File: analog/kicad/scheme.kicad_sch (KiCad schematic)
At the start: 25 parts, among them J1 Barrel_Jack_Switch, U1 LM7805_TO220, U2 LM324

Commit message: more ai research + kicad schematic update
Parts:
- removed J1: Barrel_Jack_Switch, Connector_BarrelJack:BarrelJack_GCT_DCJ200-10-A_Horizontal, symbol Connector:Barrel_Jack_Switch
- removed R7: 1.6k, Resistor_SMD:R_0805_2012Metric, symbol Device:R
- removed R8: 4.7k, Resistor_SMD:R_0805_2012Metric, symbol Device:R
- added BT1: Battery_Cell 9V, Battery:BatteryClip_Keystone_54_D16-19mm, symbol Device:Battery_Cell
- added SW1: SW_Nidec_CAS-120A1, Button_Switch_SMD:Nidec_Copal_CAS-120A, symbol Switch:SW_Nidec_CAS-120A1
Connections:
- net +5V: now also R3.1; no longer R3.2
- net GND: now also C2.2, R1.2, U1.2 (GND), BT1.2 (-); no longer C2.1, R1.1
- net at C3.1, U1.1 (VI): now also SW1.3 (A)
- removed net BIAS: C2.2, R1.2, R3.1, U2.3 (+)
- net OUT renamed TIA_OUT
- net dist2 renamed (1.7V)
- net dist3 renamed (2.5V)
- new net: BT1.1 (+), SW1.2 (B)
- new net VGND: C2.1, R1.1, R3.2, U2.3 (+)
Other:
- note added: "Authors: Uko Poschlin Karl Romet de La Torre Jüri Kajava"
- moved on the sheet: C1, C2, C3, C4, C5, D1, D2, D3, D4, D5, R1, R10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

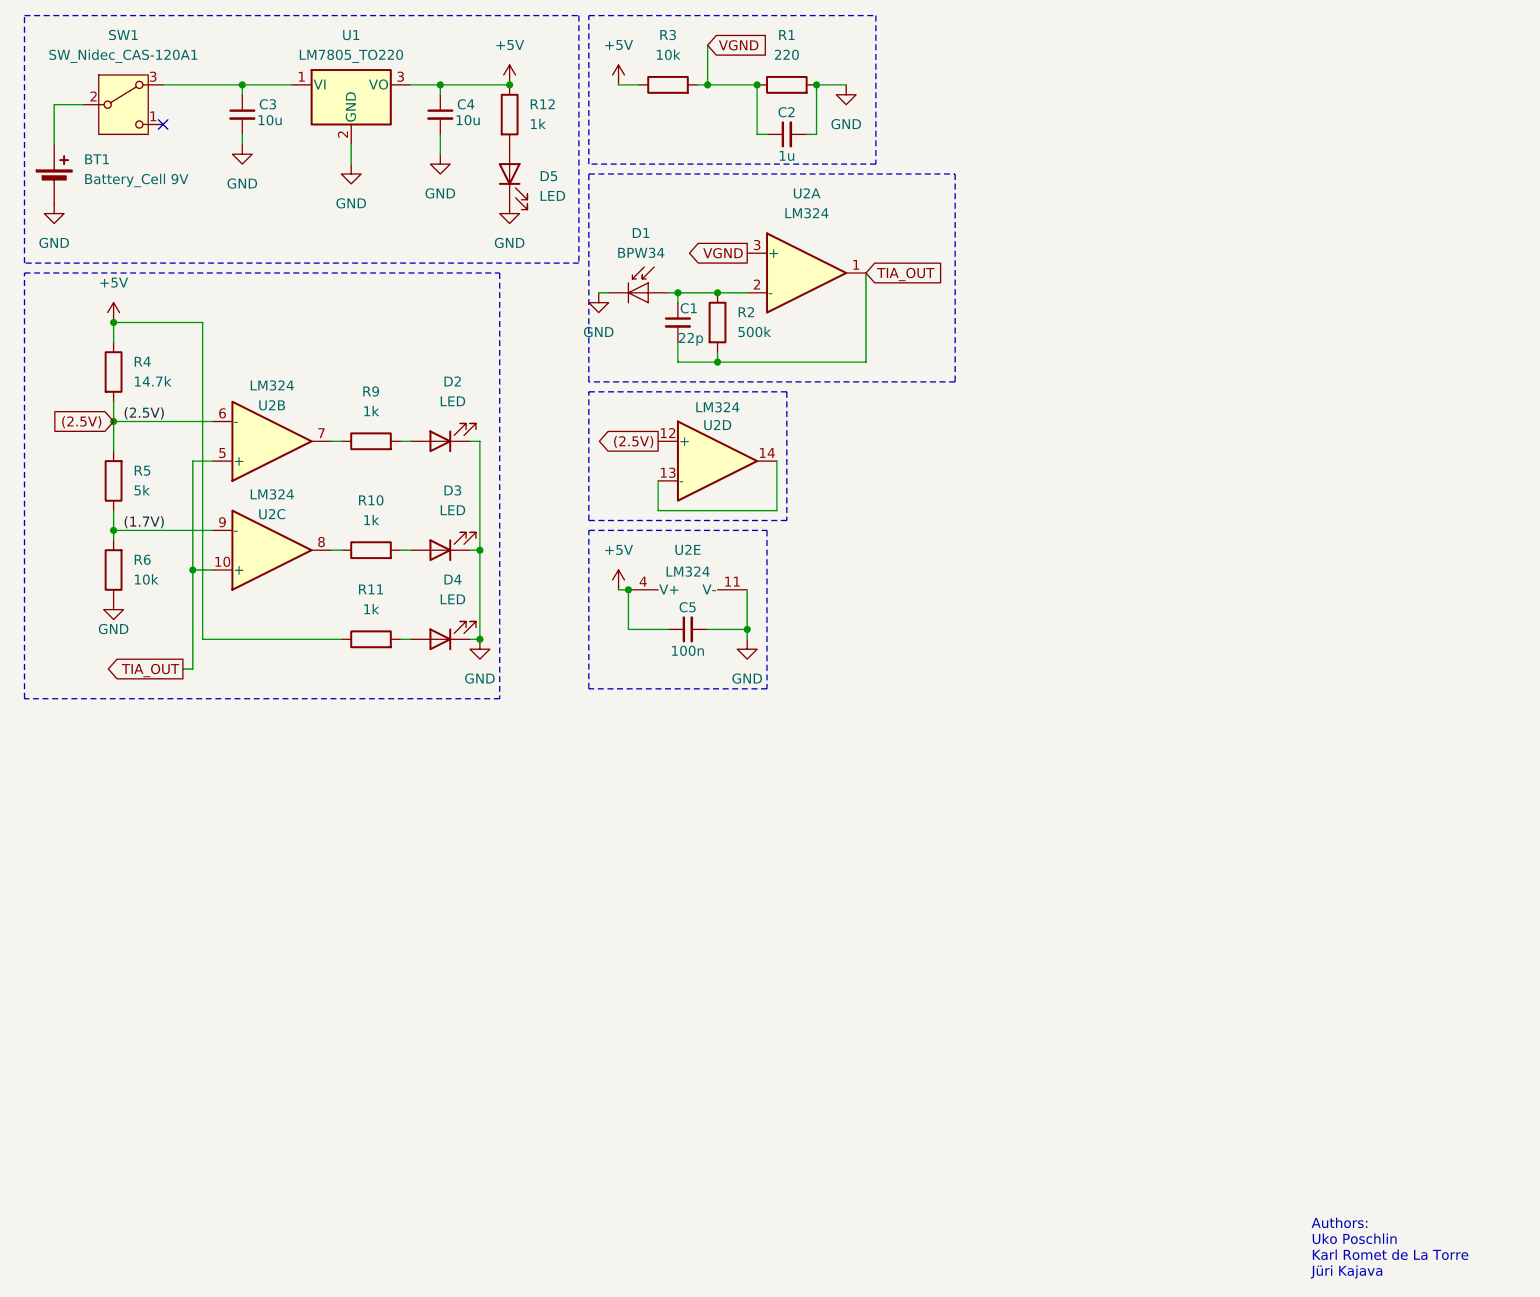
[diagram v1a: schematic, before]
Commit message: + fuse + tvs
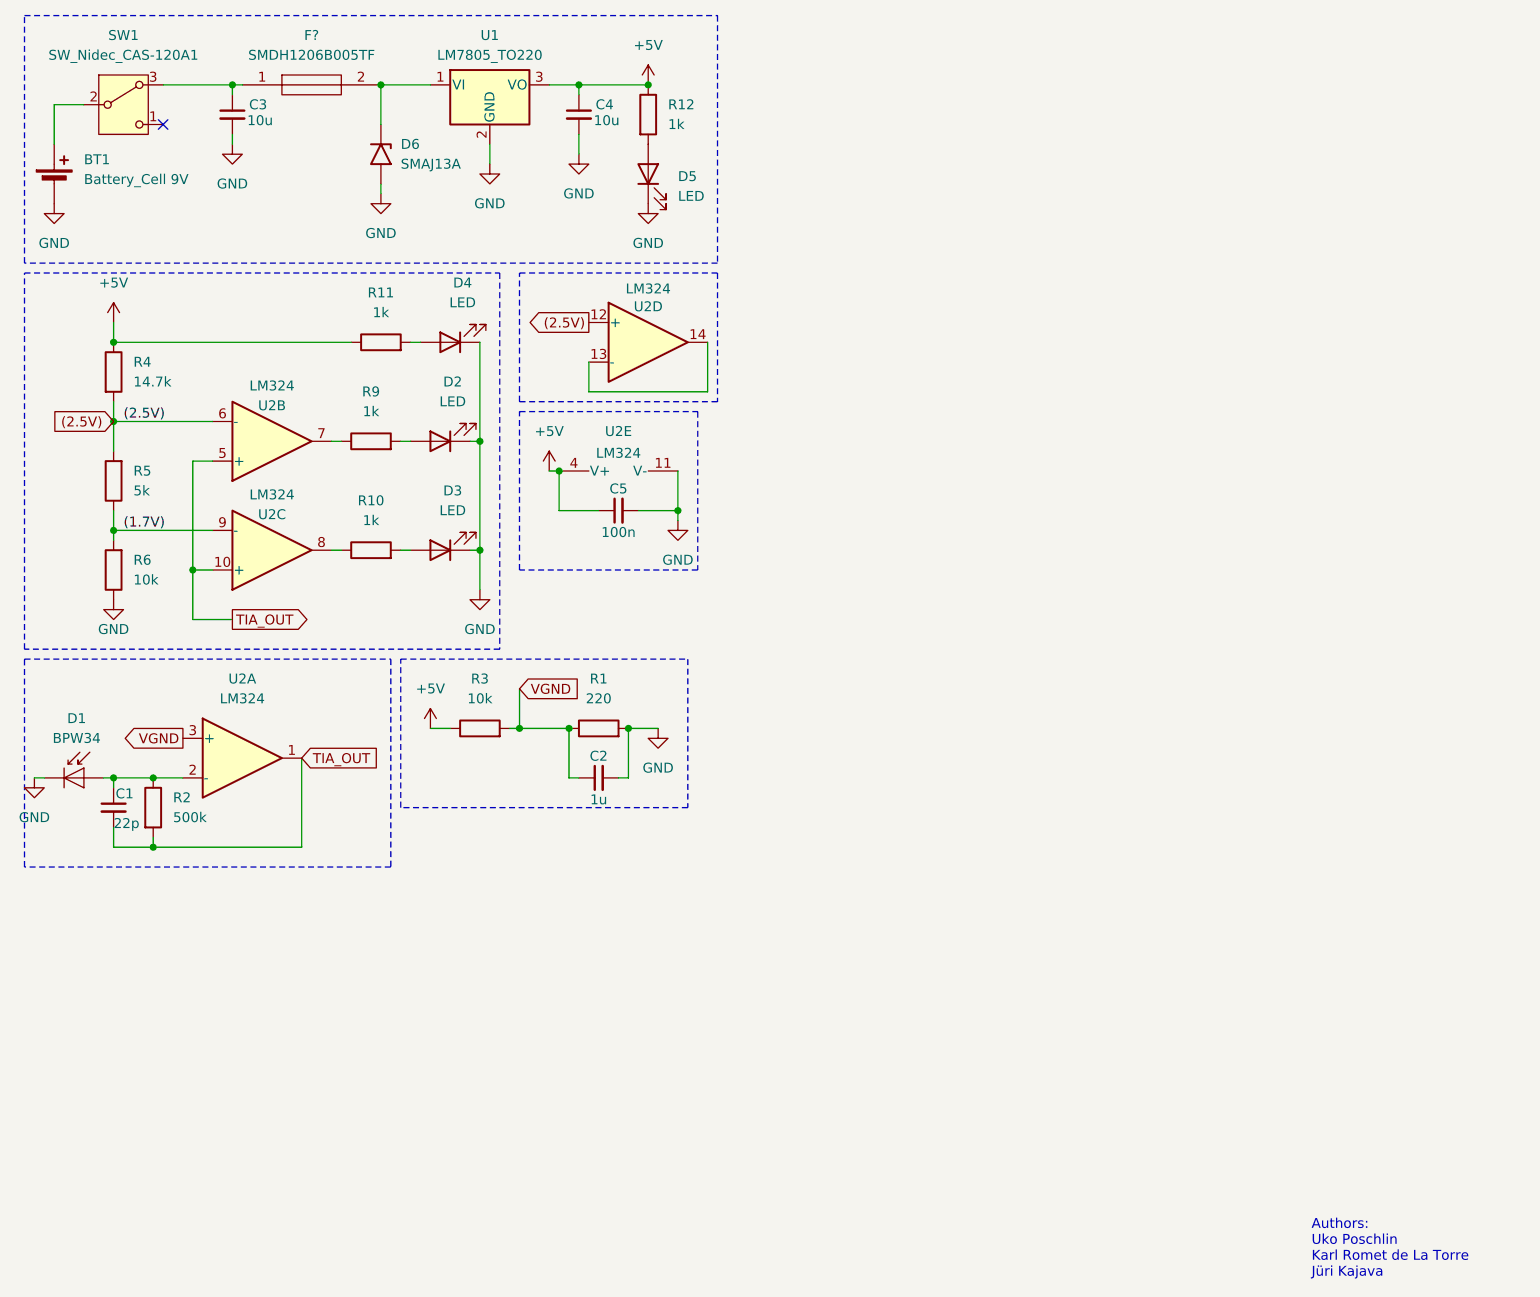
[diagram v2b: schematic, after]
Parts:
- added D6: SMAJ13A, Diode_SMD:D_SMA, symbol Diode:SMAJ13A
- added F?: SMDH1206B005TF, FUSC3216X115N, symbol IMPORT_LIB:SMDH1206B005TF
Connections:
- net GND: now also D6.2 (A2)
- net at C3.1, SW1.3 (A): now also F?.1; no longer U1.1 (VI)
- new net: D6.1 (A1), F?.2, U1.1 (VI)
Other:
- moved on the sheet: C1, C2, C3, C4, C5, D1, D4, D5, R1, R11, R12, R2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

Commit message: pcb changes
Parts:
- BT1: footprint Battery:BatteryClip_Keystone_54_D16-19mm -> Battery:BatteryHolder_Eagle_12BH611-GR
- F1: renamed from F?; footprint FUSC3216X115N -> Resistor_SMD:R_1206_3216Metric
- U2: footprint Package_DIP:DIP-14_W7.62mm_Socket -> Package_DIP:DIP-14_W7.62mm_SMDSocket_SmallPads
- renumbered R12 to R10, R9 to R7, R10 to R8, R11 to R9
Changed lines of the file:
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@@
 		(dnp no)
 		(fields_autoplaced yes)
-		(property "Reference" "R12"
+		(property "Reference" "R10"
 			(at 95.25 24.1299 0)
 			(effects
@@
 			(project ""
 				(path "/592a964a-3b7b-4079-9a16-282b0fdb7c03"
-					(reference "R12")
+					(reference "R10")
 					(unit 1)
 				)
@@
 		(dnp no)
 		(fields_autoplaced yes)
-		(property "Reference" "R10"
+		(property "Reference" "R8"
 			(at 57.15 74.93 90)
 			(effects
@@
 			(project "scheme"
 				(path "/592a964a-3b7b-4079-9a16-282b0fdb7c03"
-					(reference "R10")
+					(reference "R8")
 					(unit 1)
 				)
@@
 			)
 		)
-		(property "Footprint" "Battery:BatteryClip_Keystone_54_D16-19mm"
+		(property "Footprint" "Battery:BatteryHolder_Eagle_12BH611-GR"
 			(at 16.51 32.766 90)
 			(effects
@@
 			)
 		)
-		(property "Footprint" "Package_DIP:DIP-14_W7.62mm_Socket"
+		(property "Footprint" "Package_DIP:DIP-14_W7.62mm_SMDSocket_SmallPads"
 			(at 91.44 52.07 0)
 			(effects
@@
 		(dnp no)
 		(fields_autoplaced yes)
-		(property "Reference" "R11"
+		(property "Reference" "R9"
 			(at 58.42 48.26 90)
 			(effects
@@
 			(project "scheme"
 				(path "/592a964a-3b7b-4079-9a16-282b0fdb7c03"
-					(reference "R11")
+					(reference "R9")
 					(unit 1)
 				)
@@
 		(dnp no)
 		(fields_autoplaced yes)
-		(property "Reference" "F?"
+		(property "Reference" "F1"
 			(at 49.53 15.24 0)
 			(effects
@@
 			)
 		)
-		(property "Footprint" "FUSC3216X115N"
+		(property "Footprint" "Resistor_SMD:R_1206_3216Metric"
 			(at 54.61 20.32 0)
 			(effects
@@
 			(project ""
 				(path "/592a964a-3b7b-4079-9a16-282b0fdb7c03"
-					(reference "F?")
+					(reference "F1")
 					(unit 1)
 				)
@@
 			)
 		)
-		(property "Footprint" "Package_DIP:DIP-14_W7.62mm_Socket"
+		(property "Footprint" "Package_DIP:DIP-14_W7.62mm_SMDSocket_SmallPads"
 			(at 39.37 105.41 0)
 			(effects
@@
 			)
 		)
-		(property "Footprint" "Package_DIP:DIP-14_W7.62mm_Socket"
+		(property "Footprint" "Package_DIP:DIP-14_W7.62mm_SMDSocket_SmallPads"
 			(at 43.18 83.82 0)
 			(effects
@@
 		(dnp no)
 		(fields_autoplaced yes)
-		(property "Reference" "R9"
+		(property "Reference" "R7"
 			(at 57.15 60.96 90)
 			(effects
@@
 			(project "scheme"
 				(path "/592a964a-3b7b-4079-9a16-282b0fdb7c03"
-					(reference "R9")
+					(reference "R7")
 					(unit 1)
 				)
@@
 			)
 		)
-		(property "Footprint" "Package_DIP:DIP-14_W7.62mm_Socket"
+		(property "Footprint" "Package_DIP:DIP-14_W7.62mm_SMDSocket_SmallPads"
 			(at 43.18 69.85 0)
 			(effects
@@
 			)
 		)
-		(property "Footprint" "Package_DIP:DIP-14_W7.62mm_Socket"
+		(property "Footprint" "Package_DIP:DIP-14_W7.62mm_SMDSocket_SmallPads"
 			(at 86.36 69.85 0)
 			(effects

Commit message: more analog cleanup
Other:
- note removed: "Authors: Uko Poschlin Karl Romet de La Torre Jüri Kajava"
- company: (none) -> Uko Poschlin; Karl Romet de la Torre;
- title: (none) -> Valgustugevuse mõõtmine fotodioodiga 
- moved on the sheet: BT1, C1, C2, C3, C4, C5, D1, D2, D3, D4, D5, D6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

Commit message: pcb changes
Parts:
- D2, D3, D4: footprint LED_THT:LED_D5.0mm -> LED_THT:LED_D5.0mm_Horizontal_O1.27mm_Z3.0mm
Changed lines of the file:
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@@
 			)
 		)
-		(property "Footprint" "LED_THT:LED_D5.0mm"
+		(property "Footprint" "LED_THT:LED_D5.0mm_Horizontal_O1.27mm_Z3.0mm"
 			(at 82.55 107.95 0)
 			(effects
@@
 			)
 		)
-		(property "Footprint" "LED_THT:LED_D5.0mm"
+		(property "Footprint" "LED_THT:LED_D5.0mm_Horizontal_O1.27mm_Z3.0mm"
 			(at 82.55 121.92 0)
 			(effects
@@
 			)
 		)
-		(property "Footprint" "LED_THT:LED_D5.0mm"
+		(property "Footprint" "LED_THT:LED_D5.0mm_Horizontal_O1.27mm_Z3.0mm"
 			(at 83.82 95.25 0)
 			(effects

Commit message: bom changes
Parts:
- BT1: Mouser Price/Stock (none) -> 1,46
- C1, C2: Mouser Price/Stock (none) -> 0,10
- C3, C4: Mouser Price/Stock (none) -> 0,16
- C5: Mouser Price/Stock (none) -> 0,06
- D1: Mouser Price/Stock (none) -> 1,06
- D6: Mouser Price/Stock (none) -> 0,12
- F1: Mouser Price/Stock (none) -> 0,09
- SW1: Mouser Price/Stock (none) -> 1,26
- U1: Mouser Price/Stock (none) -> 1,55
- U2: Mouser Price/Stock (none) -> 0,404
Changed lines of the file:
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@@
+			)
+		)
+		(property "Mouser Price/Stock" "0,12"
+			(at 74.93 71.12 90)
+			(effects
+				(font
+					(size 1.27 1.27)
+				)
+				(hide yes)
 			)
 		)
@@
 			)
 		)
-		(property "Datasheet" "~"
+		(property "Datasheet" "https://mm.digikey.com/Volume0/opasdata/d220001/medias/docus/5660/3372_0805B105J250CC.pdf"
 			(at 102.87 151.13 0)
 			(effects
@@
 		(property "Description" "Unpolarized capacitor, small symbol"
 			(at 102.87 151.13 0)
+			(effects
+				(font
+					(size 1.27 1.27)
+				)
+				(hide yes)
+			)
+		)
+		(property "Mouser Price/Stock" "0,10"
+			(at 102.87 151.13 90)
 			(effects
 				(font
@@
 			)
 		)
-		(property "Datasheet" "~"
+		(property "Datasheet" "https://mm.digikey.com/Volume0/opasdata/d220001/medias/docus/5660/3372_0805W106K6R3CC.pdf"
 			(at 55.88 66.04 0)
 			(effects
@@
 		)
 		(property "Description" "Unpolarized capacitor, small symbol"
+			(at 55.88 66.04 0)
+			(effects
+				(font
+					(size 1.27 1.27)
+				)
+				(hide yes)
+			)
+		)
+		(property "Mouser Price/Stock" "0,16"
 			(at 55.88 66.04 0)
 			(effects
@@
 			)
 		)
+		(property "Mouser Price/Stock" "1,26"
+			(at 41.91 64.77 0)
+			(effects
+				(font
+					(size 1.27 1.27)
+				)
+				(hide yes)
+			)
+		)
 		(pin "3"
 		)
@@
 			)
 		)
+		(property "Mouser Price/Stock" "1,06"
+			(at 36.83 151.13 0)
+			(effects
+				(font
+					(size 1.27 1.27)
+				)
+				(hide yes)
+			)
+		)
 		(pin "1"
 		)
@@
 			)
 		)
-		(property "Datasheet" "~"
+		(property "Datasheet" "https://mm.digikey.com/Volume0/opasdata/d220001/medias/docus/5491/0805B104K201DC.pdf"
 			(at 105.41 116.84 0)
 			(effects
@@
 		(property "Description" "Unpolarized capacitor, small symbol"
 			(at 105.41 116.84 0)
+			(effects
+				(font
+					(size 1.27 1.27)
+				)
+				(hide yes)
+			)
+		)
+		(property "Mouser Price/Stock" "0,06"
+			(at 105.41 116.84 90)
 			(effects
 				(font
@@
 			)
 		)
-		(property "Datasheet" "~"
+		(property "Datasheet" "https://www.mouser.com/catalog/specsheets/EPD-200766.pdf?_gl=1*f86mo4*_gcl_au*MTA2MTk2OTIxNC4xNzY0NzA2NDYw*_ga*MTk3OTE1MDk4OS4xNzY0NzA2NDYy*_ga_15W4STQT4T*czE3NjQ3MDY0NjEkbzEkZzAkdDE3NjQ3MDY0NjQkajU3JGwwJGgw"
 			(at 33.02 73.406 90)
 			(effects
@@
 		)
 		(property "Description" "Single-cell battery"
+			(at 33.02 74.93 0)
+			(effects
+				(font
+					(size 1.27 1.27)
+				)
+				(hide yes)
+			)
+		)
+		(property "Mouser Price/Stock" "1,46"
 			(at 33.02 74.93 0)
 			(effects
@@
 			)
 		)
+		(property "Mouser Price/Stock" "0,404"
+			(at 109.22 95.25 0)
+			(effects
+				(font
+					(size 1.27 1.27)
+				)
+				(hide yes)
+			)
+		)
 		(pin "1"
 		)
@@
 			)
 		)
-		(property "Mouser Price/Stock" ""
+		(property "Mouser Price/Stock" "0,09"
 			(at 71.12 73.66 0)
 			(effects
@@
 			)
 		)
+		(property "Mouser Price/Stock" "1,55"
+			(at 88.9 62.23 0)
+			(effects
+				(font
+					(size 1.27 1.27)
+				)
+				(hide yes)
+			)
+		)
 		(pin "1"
 		)
@@
 			)
 		)
+		(property "Mouser Price/Stock" "0,404"
+			(at 57.15 148.59 0)
+			(effects
+				(font
+					(size 1.27 1.27)
+				)
+				(hide yes)
+			)
+		)
 		(pin "1"
 		)
@@
 			)
 		)
-		(property "Datasheet" "~"
+		(property "Datasheet" "https://mm.digikey.com/Volume0/opasdata/d220001/medias/docus/5534/CL21C220JB61PNC%20Spec.pdf"
 			(at 40.64 154.94 0)
 			(effects
@@
 		)
 		(property "Description" "Unpolarized capacitor, small symbol"
+			(at 40.64 154.94 0)
+			(effects
+				(font
+					(size 1.27 1.27)
+				)
+				(hide yes)
+			)
+		)
+		(property "Mouser Price/Stock" "0,10"
 			(at 40.64 154.94 0)
 			(effects
@@
 			)
 		)
+		(property "Mouser Price/Stock" "0,404"
+			(at 60.96 121.92 0)
+			(effects
+				(font
+					(size 1.27 1.27)
+				)
+				(hide yes)
+			)
+		)
 		(pin "1"
 		)
@@
 			)
 		)
+		(property "Mouser Price/Stock" "0,404"
+			(at 60.96 107.95 0)
+			(effects
+				(font
+					(size 1.27 1.27)
+				)
+				(hide yes)
+			)
+		)
 		(pin "1"
 		)
@@
 			)
 		)
+		(property "Mouser Price/Stock" "0,404"
+			(at 105.41 109.22 90)
+			(effects
+				(font
+					(size 1.27 1.27)
+				)
+				(hide yes)
+			)
+		)
 		(pin "1"
 		)
@@
 			)
 		)
-		(property "Datasheet" "~"
+		(property "Datasheet" "https://mm.digikey.com/Volume0/opasdata/d220001/medias/docus/5660/3372_0805W106K6R3CC.pdf"
 			(at 100.33 66.04 0)
 			(effects
@@
 			(at 100.33 66.04 0)
 			(effects
+				(font
+					(size 1.27 1.27)
+				)
+				(hide yes)
+			)
+		)
+		(property "Mouser Price/Stock" "0,16"
+			(at 100.33 66.04 0)
+			(effects

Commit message: schem image
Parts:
- BT1: value Battery_Cell 9V -> 9
- D1: value BPW34 -> ${SIM.PARAMS}
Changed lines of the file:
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@@
 			)
 		)
-		(property "Sim.Pins" "1=K 2=A"
+		(property "Sim.Pins" "1=A 2=K"
+			(at 82.55 107.95 0)
+			(effects
+				(font
+					(size 1.27 1.27)
+				)
+				(hide yes)
+			)
+		)
+		(property "Sim.Device" "D"
 			(at 82.55 107.95 0)
 			(effects
@@
 			)
 		)
+		(property "Sim.Device" "TLINE"
+			(at 41.91 64.77 0)
+			(effects
+				(font
+					(size 1.27 1.27)
+				)
+				(hide yes)
+			)
+		)
+		(property "Sim.Pins" "1=1+ 2=1- 3=2+"
+			(at 41.91 64.77 0)
+			(effects
+				(font
+					(size 1.27 1.27)
+				)
+				(hide yes)
+			)
+		)
+		(property "Sim.Params" "z0=0 td=0"
+			(at 41.91 64.77 0)
+			(effects
+				(font
+					(size 1.27 1.27)
+				)
+				(hide yes)
+			)
+		)
 		(pin "3"
 		)
@@
 			)
 		)
-		(property "Value" "BPW34"
+		(property "Value" "${SIM.PARAMS}"
 			(at 35.9029 146.05 0)
 			(effects
@@
 		)
 		(property "Mouser Price/Stock" "1,06"
+			(at 36.83 151.13 0)
+			(effects
+				(font
+					(size 1.27 1.27)
+				)
+				(hide yes)
+			)
+		)
+		(property "Sim.Device" "I"
+			(at 36.83 151.13 0)
+			(effects
+				(font
+					(size 1.27 1.27)
+				)
+				(hide yes)
+			)
+		)
+		(property "Sim.Type" "DC"
+			(at 36.83 151.13 0)
+			(effects
+				(font
+					(size 1.27 1.27)
+				)
+				(hide yes)
+			)
+		)
+		(property "Sim.Pins" "1=+ 2=-"
+			(at 36.83 151.13 0)
+			(effects
+				(font
+					(size 1.27 1.27)
+				)
+				(hide yes)
+			)
+		)
+		(property "Sim.Params" "dc=0.001"
 			(at 36.83 151.13 0)
 			(effects
@@
 			)
 		)
-		(property "Sim.Pins" "1=K 2=A"
+		(property "Sim.Pins" "1=A 2=K"
+			(at 109.22 73.66 0)
+			(effects
+				(font
+					(size 1.27 1.27)
+				)
+				(hide yes)
+			)
+		)
+		(property "Sim.Device" "D"
 			(at 109.22 73.66 0)
 			(effects
@@
 		(on_board yes)
 		(dnp no)
-		(fields_autoplaced yes)
 		(property "Reference" "R10"
 			(at 111.76 64.7699 0)
@@
 		(property "Description" "Resistor"
 			(at 109.22 66.04 0)
+			(effects
+				(font
+					(size 1.27 1.27)
+				)
+				(hide yes)
+			)
+		)
+		(property "Sim.Device" "R"
+			(at 116.078 44.196 0)
+			(effects
+				(font
+					(size 1.27 1.27)
+				)
+				(hide yes)
+			)
+		)
+		(property "Sim.Pins" "1=+ 2=-"
+			(at 116.078 44.196 0)
 			(effects
 				(font
@@
 			)
 		)
-		(property "Sim.Pins" "1=K 2=A"
+		(property "Sim.Pins" "1=A 2=K"
+			(at 82.55 121.92 0)
+			(effects
+				(font
+					(size 1.27 1.27)
+				)
+				(hide yes)
+			)
+		)
+		(property "Sim.Device" "D"
 			(at 82.55 121.92 0)
 			(effects
@@
 			)
 		)
-		(property "Value" "Battery_Cell 9V"
+		(property "Value" "9"
 			(at 36.83 74.3584 0)
 			(effects
@@
 		)
 		(property "Mouser Price/Stock" "1,46"
+			(at 33.02 74.93 0)
+			(effects
+				(font
+					(size 1.27 1.27)
+				)
+				(hide yes)
+			)
+		)
+		(property "Sim.Device" "V"
+			(at 33.02 74.93 0)
+			(effects
+				(font
+					(size 1.27 1.27)
+				)
+				(hide yes)
+			)
+		)
+		(property "Sim.Type" "DC"
+			(at 33.02 74.93 0)
+			(effects
+				(font
+					(size 1.27 1.27)
+				)
+				(hide yes)
+			)
+		)
+		(property "Sim.Pins" "1=+ 2=-"
 			(at 33.02 74.93 0)
 			(effects
@@
 			)
 		)
-		(property "Sim.Pins" "1=K 2=A"
+		(property "Sim.Device" "SPICE"
+			(at 83.82 95.25 0)
+			(effects
+				(font
+					(size 1.27 1.27)
+				)
+				(hide yes)
+			)
+		)
+		(property "Sim.Params" "model=\".model DLED D(Is=2e-9 N=2.0 Rs=10 Cjo=2p M=0.5 Eg=1.8 Bv=5 Ibv=0.1u)\""
 			(at 83.82 95.25 0)
 			(effects
@@
 			(at 45.72 154.94 0)
 			(effects
+				(font
+					(size 1.27 1.27)
+				)
+				(hide yes)
+			)
+		)
+		(property "Sim.Device" "R"
+			(at 45.72 154.94 0)
+			(effects
+				(font
+					(size 1.27 1.27)
+				)
+				(hide yes)
+			)
+		)
+		(property "Sim.Pins" "1=+ 2=-"
+			(at 45.72 154.94 0)
+			(effects

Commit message: got simulation running
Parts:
- D1: value ${SIM.PARAMS} -> 0.001
- F1: value SMDH1206B005TF -> ${SIM.PARAMS}; type (none) -> SMDH1206B005TF
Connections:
- net (2.5V) renamed (+2.5V)
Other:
- moved on the sheet: D4, R9
